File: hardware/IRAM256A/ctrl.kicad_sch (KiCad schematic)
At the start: 3 parts

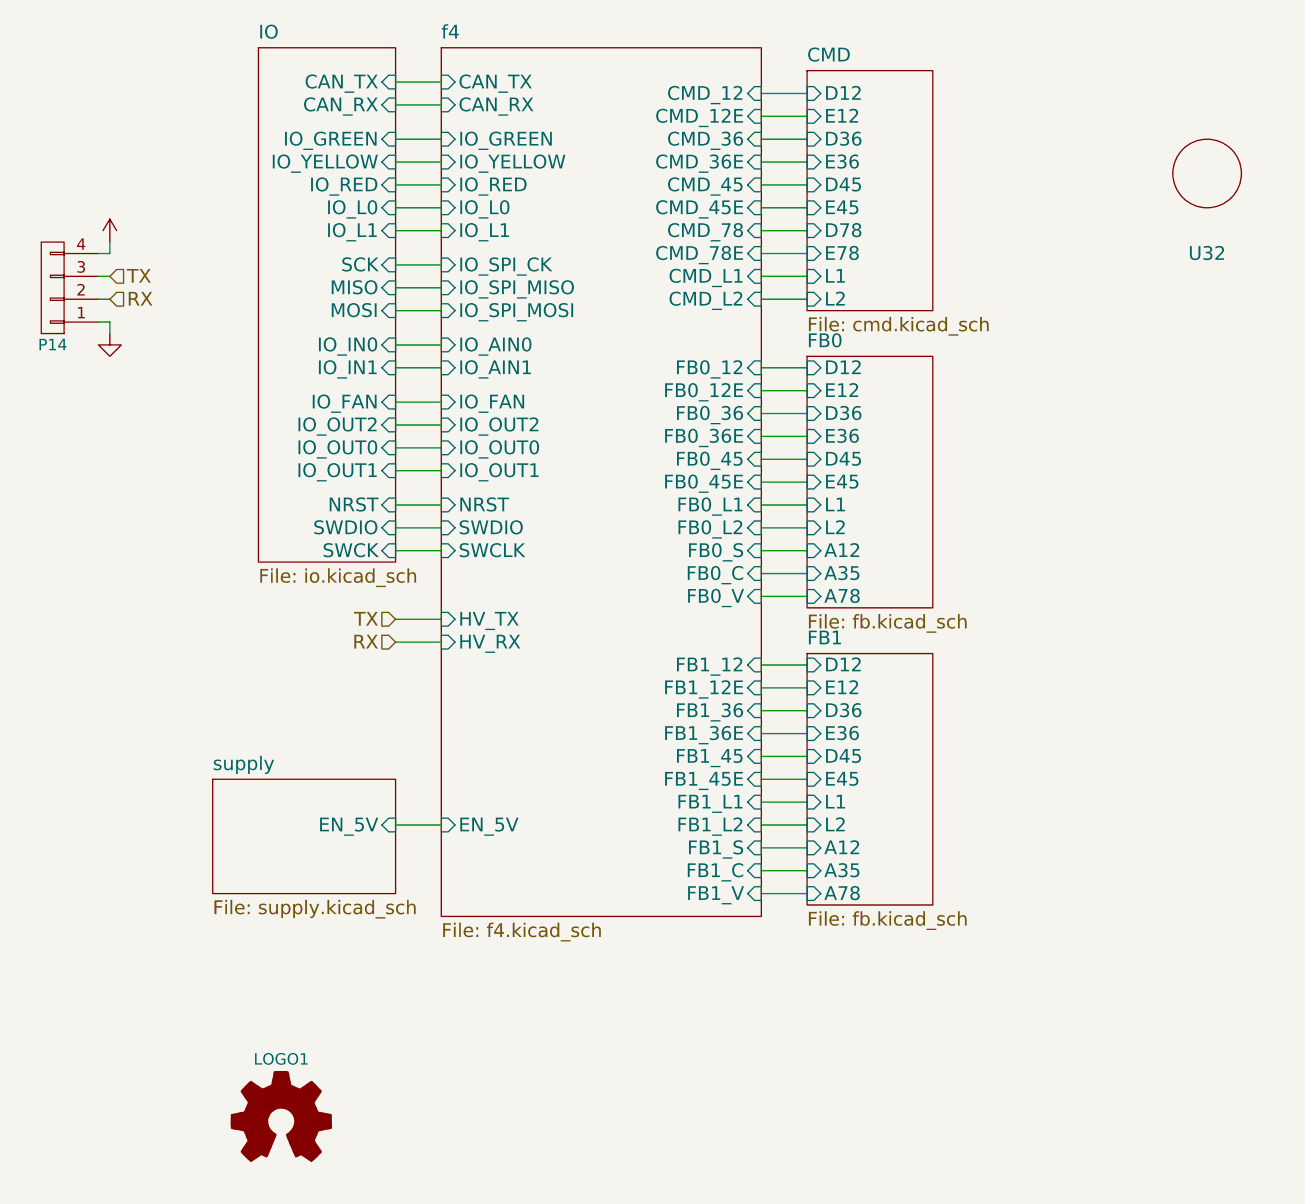
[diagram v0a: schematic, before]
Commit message: Structure change + kicad 3d models updated
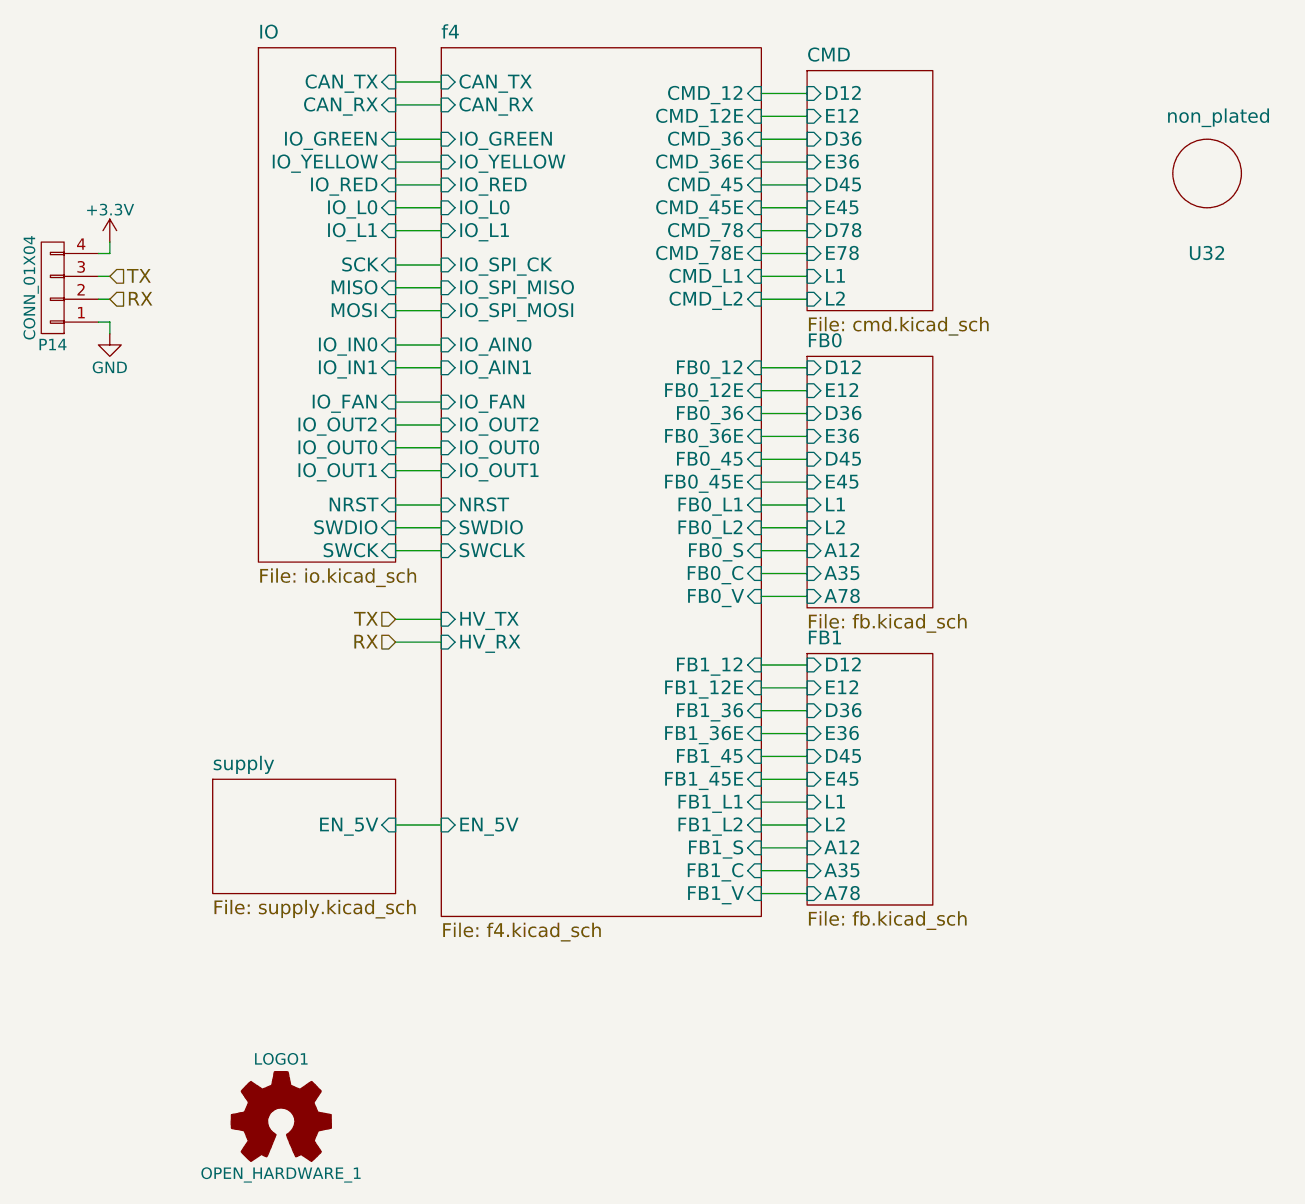
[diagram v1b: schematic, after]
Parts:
- LOGO1: value (none) -> OPEN_HARDWARE_1; footprint (none) -> stmbl:Symbol_OSHW-Logo_SilkScreen
- P14: value (none) -> CONN_01X04; footprint (none) -> stmbl:Pin_Header_Angled_1x04
- U32: value (none) -> non_plated; footprint (none) -> stmbl:non_plated_3mm
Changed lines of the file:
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@@
       (effects (font (size 1.27 1.27)) hide)
     )
-    (property "Value" "" (id 1) (at 41.91 35.814 0))
+    (property "Value" "+3.3V" (id 1) (at 41.91 35.814 0))
     (property "Footprint" "" (id 2) (at 41.91 39.37 0))
     (property "Datasheet" "" (id 3) (at 41.91 39.37 0))
@@
       (effects (font (size 1.27 1.27)) hide)
     )
-    (property "Value" "" (id 1) (at 41.91 53.34 0))
+    (property "Value" "GND" (id 1) (at 41.91 53.34 0))
     (property "Footprint" "" (id 2) (at 41.91 49.53 0))
     (property "Datasheet" "" (id 3) (at 41.91 49.53 0))
@@
     (in_bom yes) (on_board yes)
     (property "Reference" "P14" (id 0) (at 35.56 50.8 0))
-    (property "Value" "" (id 1) (at 33.02 44.45 90))
-    (property "Footprint" "" (id 2) (at 35.56 44.45 0)
+    (property "Value" "CONN_01X04" (id 1) (at 33.02 44.45 90))
+    (property "Footprint" "stmbl:Pin_Header_Angled_1x04" (id 2) (at 35.56 44.45 0)
       (effects (font (size 1.27 1.27)) hide)
     )
@@
       (effects (font (size 1.524 1.524)))
     )
-    (property "Value" "" (id 1) (at 165.1 25.4 0)
+    (property "Value" "non_plated" (id 1) (at 165.1 25.4 0)
       (effects (font (size 1.524 1.524)))
     )
-    (property "Footprint" "" (id 2) (at 163.83 31.75 0)
+    (property "Footprint" "stmbl:non_plated_3mm" (id 2) (at 163.83 31.75 0)
       (effects (font (size 1.524 1.524)) hide)
     )
@@
     (in_bom yes) (on_board yes)
     (property "Reference" "LOGO1" (id 0) (at 60.96 130.175 0))
-    (property "Value" "" (id 1) (at 60.96 142.875 0))
-    (property "Footprint" "" (id 2) (at 60.96 137.16 0)
+    (property "Value" "OPEN_HARDWARE_1" (id 1) (at 60.96 142.875 0))
+    (property "Footprint" "stmbl:Symbol_OSHW-Logo_SilkScreen" (id 2) (at 60.96 137.16 0)
       (effects (font (size 1.524 1.524)) hide)
     )
